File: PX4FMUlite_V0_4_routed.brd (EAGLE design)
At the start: 48.6 x 34.9 mm, 126 parts, among them J2 DF13-4P-1.25V, J201 DF13C-6P-1.25V, J202 DF13C-6P-1.25V, J203 DF13C-6P-1.25V, J3 DF13C-4P-1.25V, J302 DF13C-4P-1.25V, J401 DF13C-4P-1.25V, J403 DF13C-7P-1.25V, J405 DF13C-4P-1.25V, J802 DF13C-3P-1.25V, M3_MOUNT1101 MOUNT-HOLE3.1MM, M3_MOUNT1102 MOUNT-HOLE3.1MM, M3_MOUNT1103 MOUNT-HOLE3.1MM, M3_MOUNT1104 MOUNT-HOLE3.1MM, U101 STM32F4X7VX, U2 MAX3051, U401 MAX3051, X101 3.2x2.5 mm / 24 MHz / 15 ppm

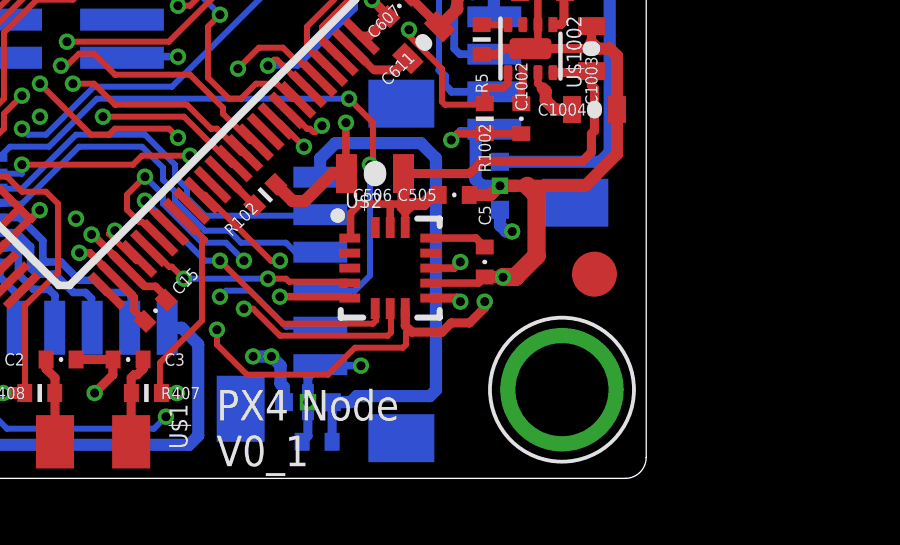
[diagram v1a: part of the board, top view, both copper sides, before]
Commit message: Added PCB Pool high spec design rules file
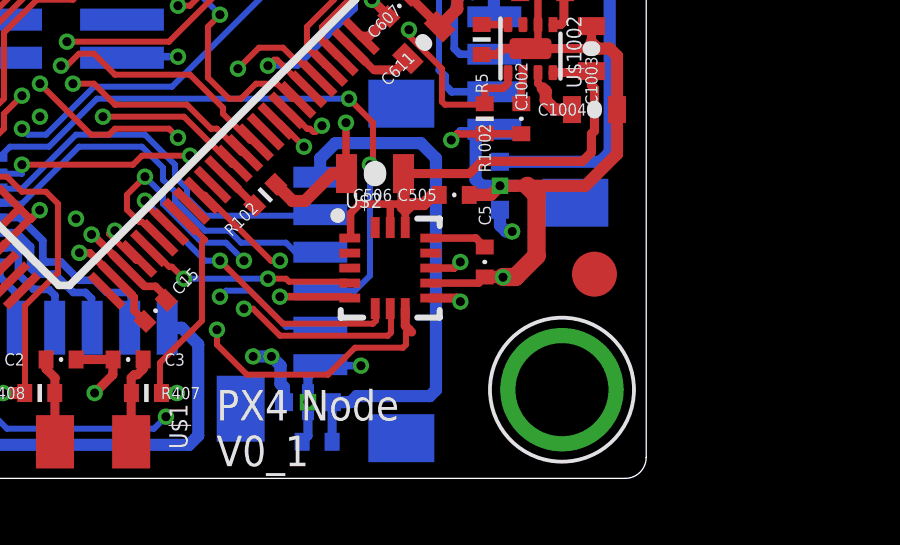
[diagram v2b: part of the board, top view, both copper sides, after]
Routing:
- net !GYRO_CS: track 37.8 -> 34.8 mm, vias 3 -> 2
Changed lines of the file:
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@@
 <wire x1="49.776" y1="7.8312" x2="49.9036" y2="7.7036" width="0.3048" layer="1"/>
 <wire x1="49.9036" y1="7.7036" x2="49.9872" y2="7.62" width="0.3048" layer="1"/>
-<wire x1="49.9872" y1="7.62" x2="51.0032" y2="7.62" width="0.3048" layer="1"/>
-<wire x1="51.0032" y1="7.62" x2="51.308" y2="7.9248" width="0.3048" layer="1"/>
-<wire x1="51.308" y1="7.9248" x2="51.9176" y2="7.9248" width="0.3048" layer="1"/>
-<wire x1="51.9176" y1="7.9248" x2="52.4256" y2="8.4328" width="0.3048" layer="1"/>
-<wire x1="52.4256" y1="8.4328" x2="52.4256" y2="8.636" width="0.3048" layer="1"/>
-<via x="52.4256" y="8.636" extent="1-16" drill="0.3"/>
 <wire x1="33.2" y1="17.9" x2="30.7" y2="15.4" width="0.2" layer="1"/>
 <wire x1="33.4" y1="17.9" x2="33.2" y2="17.9" width="0.2" layer="1"/>
@@
 <via x="42.2" y="16.8" extent="1-16" drill="0.3"/>
 <via x="38.5" y="19.3" extent="1-16" drill="0.3"/>
-<wire x1="22.2" y1="23.6" x2="22.253" y2="23.968" width="0" layer="19" extent="1-1"/>
-<wire x1="22.253" y1="23.168" x2="22.253" y2="23.568" width="0" layer="19" extent="1-1"/>
-<wire x1="22.253" y1="22.768" x2="22.253" y2="23.168" width="0" layer="19" extent="1-1"/>
 </signal>
 <signal name="N$4">
